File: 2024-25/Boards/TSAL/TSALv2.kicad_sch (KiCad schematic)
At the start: 21 parts, among them J1 043045-0412, Q1 BS250P, Q2 BS170, Q3 UJ3N120035K3S, Q4 BS170, U1 H11L1M

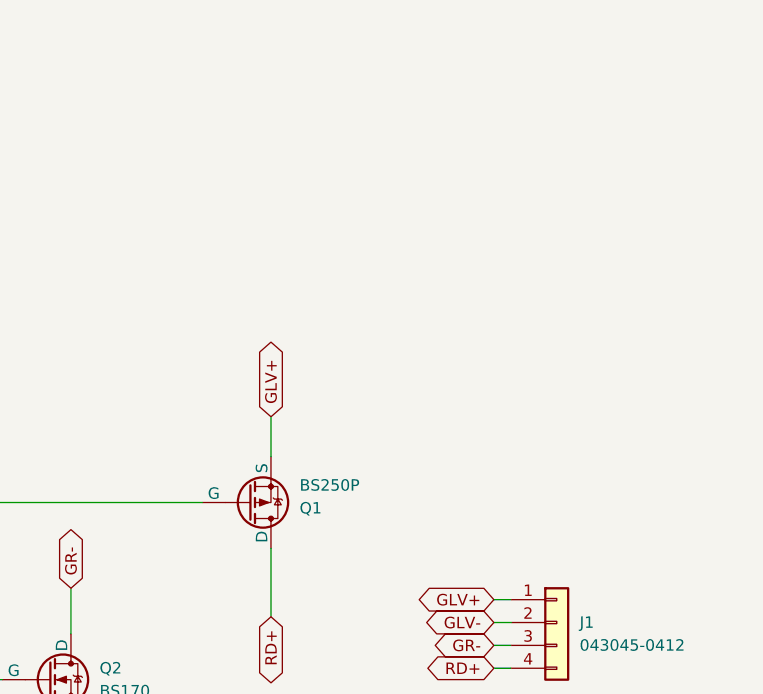
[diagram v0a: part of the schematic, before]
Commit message: added to schematic light flash
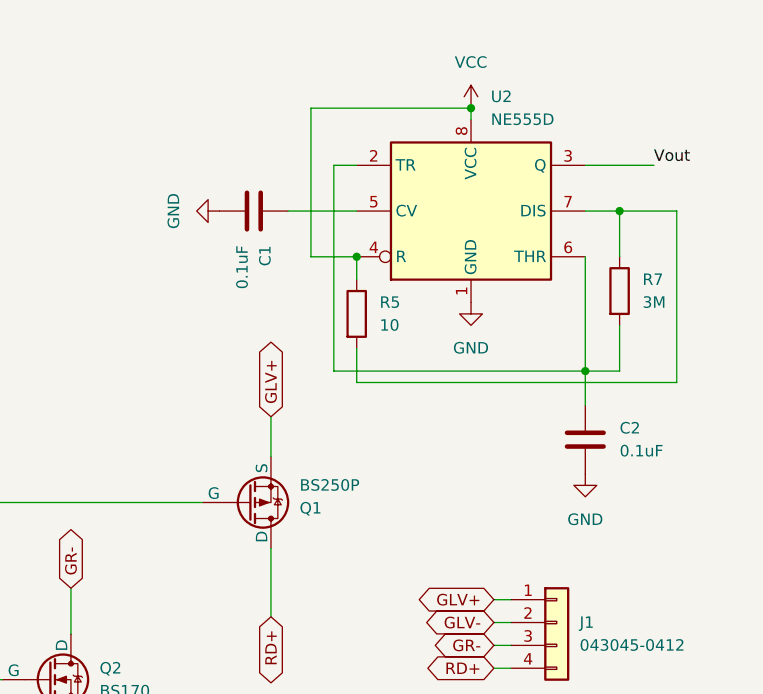
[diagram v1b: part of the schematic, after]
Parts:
- added C1, C2: 0.1uF, symbol Device:C
- added R5: 10, symbol Device:R
- added R7: 3M, symbol Device:R
- added U2: NE555D, Package_SO:SOIC-8_3.9x4.9mm_P1.27mm, symbol Timer:NE555D
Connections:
- new net: C1.2, U2.5 (CV)
- new net: C2.2, R7.2, U2.2 (TR), U2.6 (THR)
- new net: R5.2, R7.1, U2.7 (DIS)
- new net GND: C1.1, C2.1, U2.1 (GND)
- new net VCC: R5.1, U2.4 (R), U2.8 (VCC)
- new net Vout: U2.3 (Q)

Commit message: Board should be ready for pcb
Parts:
- removed Q2: BS170, Package_TO_SOT_THT:TO-92, symbol Simulation_SPICE:NMOS
- added C3: 1uF, Capacitor_SMD:C_0805_2012Metric_Pad1.18x1.45mm_HandSolder, symbol Device:C
- added C4: .1uF, Capacitor_SMD:C_0402_1005Metric_Pad0.74x0.62mm_HandSolder, symbol Device:C
- added R4: 1k, symbol Device:R
- added R8: 10k, symbol Device:R
- C2: value 0.1uF -> 100uF
- R5: value 10 -> 100
- R7: value 3M -> 3k
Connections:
- net VCC is gone; now on net GLV+: R5.1, U2.4 (R), U2.8 (VCC)
- net Vout is gone; now on net Light+: U2.3 (Q)
- net GLV+: now also Q1.1 (D), C3.2, C4.2, R4.1, R8.2
- net GLV-: no longer U1.5
- net GND: now also U1.5, C3.1, C4.1, R8.1
- net GR- renamed Light-
- net RD+ renamed Light+
- net Light+: now also R4.2; no longer Q1.1 (D)
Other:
- note removed: "LED+"
- note removed: "LED-"
- moved on the sheet: C1, C2, D10, D2, D3, D4, D5, D6, D7, D8, D9, J1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

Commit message: Add files via upload
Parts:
- removed C4: .1uF, Capacitor_SMD:C_0402_1005Metric_Pad0.74x0.62mm_HandSolder, symbol Device:C
- removed D10, D2, D3, D4, D5, D6, D7, D8, D9: BZT52-B5V6X, Diode_SMD:D_SOD-123, symbol Device:D_Zener
- removed Q1: BS250P, Package_TO_SOT_THT:TO-92, symbol Simulation_SPICE:PMOS
- removed Q4: BS170, Package_TO_SOT_THT:TO-92, symbol Simulation_SPICE:NMOS
- added D2: BZT52C12, Diode_SMD:D_SOD-123F, symbol Diode:BZT52Bxx
- added Q1: DMP2035U-7, SOT23_DIO, symbol Transistor_FET:DMP2035U-7
- added Q4: DMN2056U, Package_TO_SOT_SMD:SOT-23, symbol Transistor_FET:DMN2056U
- C1, C2: footprint (none) -> Capacitor_SMD:C_0805_2012Metric_Pad1.18x1.45mm_HandSolder
- Q3: value UJ3N120035K3S -> UJ3N065080K3S
- R1, R2, R3, R6: footprint Resistor_THT:R_Axial_DIN0207_L6.3mm_D2.5mm_P7.62mm_Horizontal -> Resistor_SMD:R_0805_2012Metric_Pad1.20x1.40mm_HandSolder
- R4, R5, R7, R8: footprint (none) -> Resistor_SMD:R_0805_2012Metric_Pad1.20x1.40mm_HandSolder
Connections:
- net GLV- is gone; now on net GND: J1.2 (Pin_2)
- net Light- is gone; now on net Light+: J1.3 (Pin_3)
- net GLV+: now also Q1.2 (S); no longer R5.1, R8.2, U2.4 (R)
- net HV+: now also D2.1 (K)
- net HV-: now also Q4.2 (S)
- net Light+: no longer J1.4 (Pin_4)
- net at R2.1: now also D2.2 (A)
- net at D1.1 (K), R2.2, R3.1: now also Q4.1 (G)
- net at U1.2: now also Q4.3 (D)
- net at R1.2, U1.4: now also Q1.1 (G)
- new net: Q1.3 (D), R5.1, R8.2, U2.4 (R)
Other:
- note removed: "Connect negative side of green LED to board and positive side of red LED"
- moved on the sheet: J1, Molex1, R8

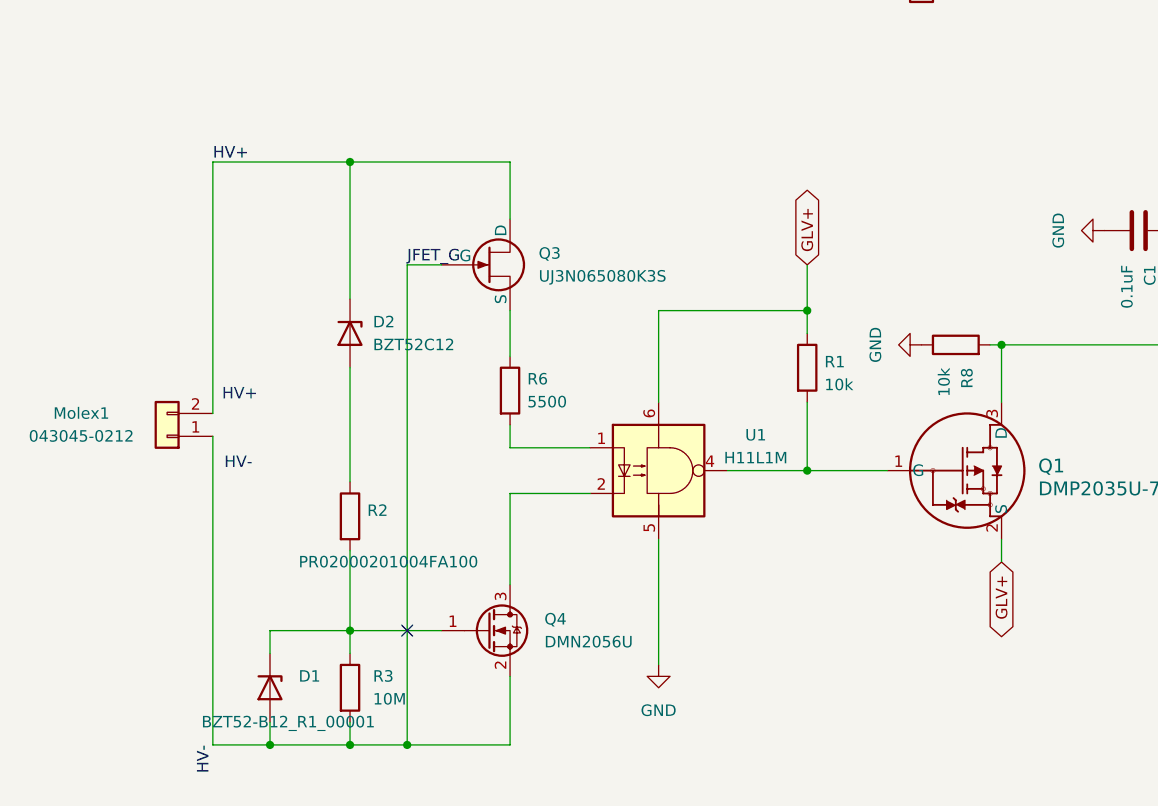
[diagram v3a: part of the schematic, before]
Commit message: split up TSAL resistors for voltage rating
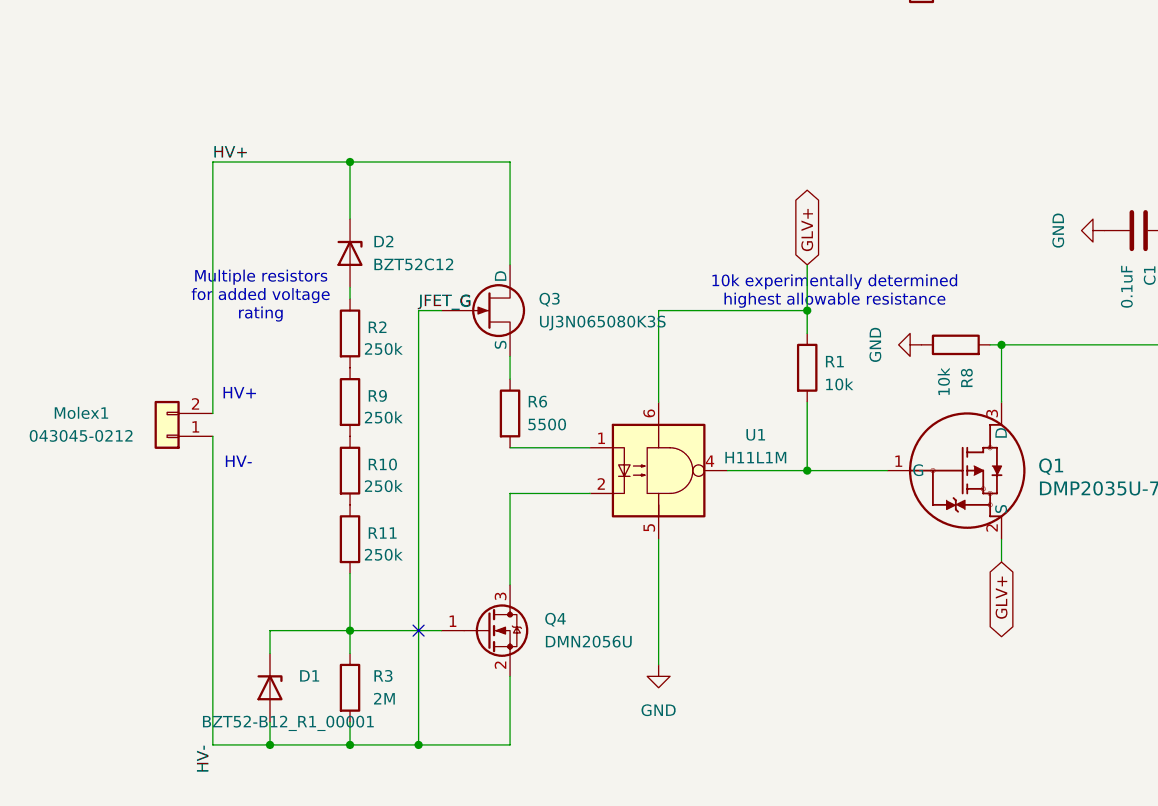
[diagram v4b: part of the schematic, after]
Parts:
- added R10, R11, R9: 250k, Resistor_SMD:R_0805_2012Metric_Pad1.20x1.40mm_HandSolder, symbol Device:R
- R2: value PR02000201004FA100 -> 250k
- R3: value 10M -> 2M
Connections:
- net at D1.1 (K), Q4.1 (G), R3.1: now also R11.2; no longer R2.2
- new net: R2.2, R9.1
- new net: R10.1, R9.2
- new net: R10.2, R11.1
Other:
- note added: "10k experimentally determined highest allowable resistance"
- note added: "Multiple resistors for added voltage rating"
- moved on the sheet: D2, Q3, R2, R6

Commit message: updated documentation
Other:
- note added: "NE555 Timer at ~3.3 Hz"
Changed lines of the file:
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@@
+		)
+	)
+	(text "NE555 Timer at ~3.3 Hz"
+		(exclude_from_sim no)
+		(at 163.576 25.4 0)
+		(effects
+			(font
+				(size 1.27 1.27)
+			)
 		)
 	)

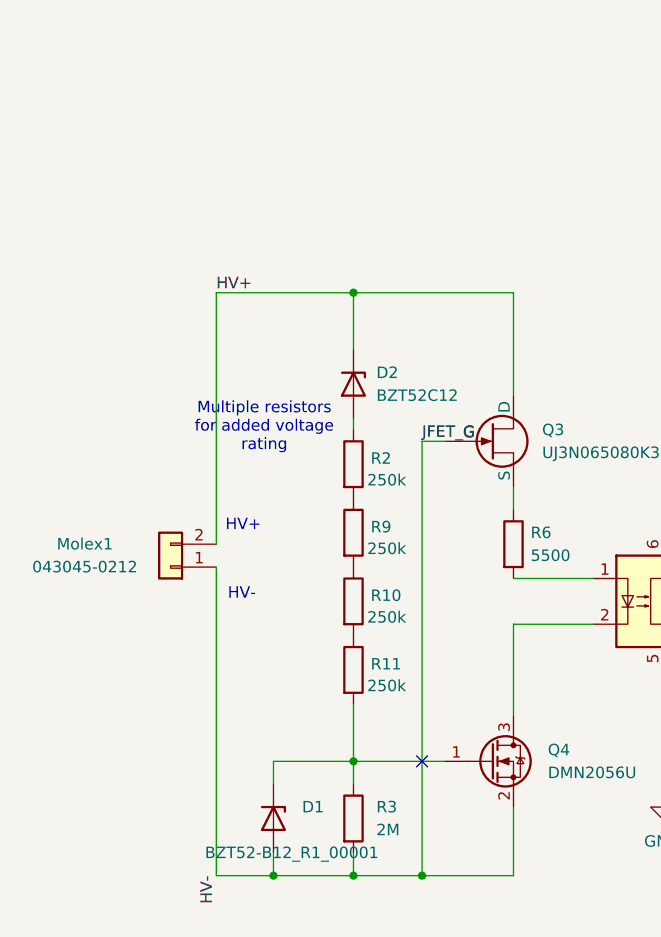
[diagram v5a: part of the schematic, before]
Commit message: updated resistors to be smd on VIL and added fuses and mounting holes to TSAL
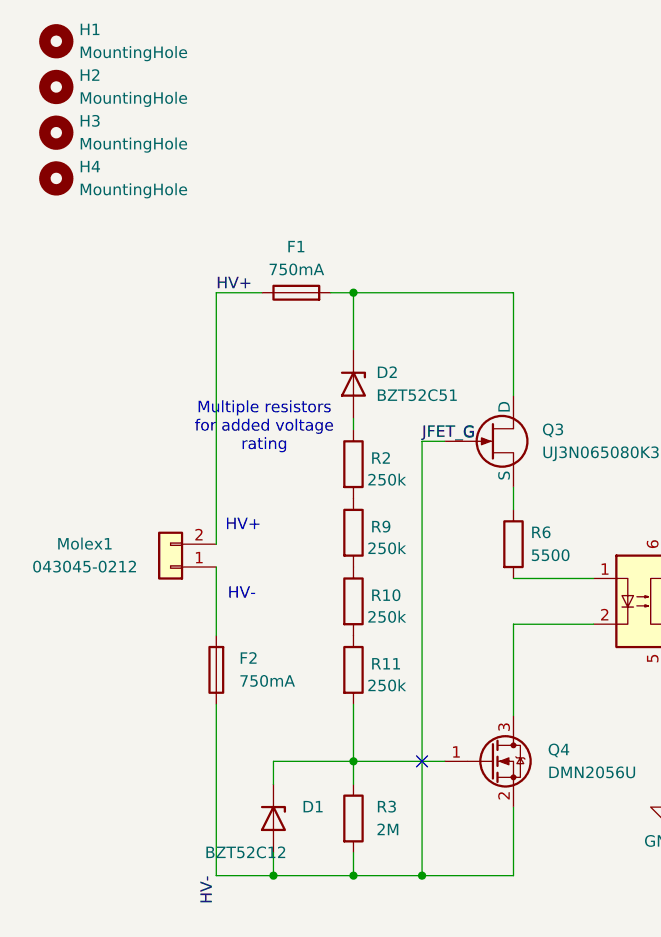
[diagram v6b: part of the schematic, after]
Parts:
- added F1, F2: 750mA, Library:FUSE_BK_PCS, symbol Device:Fuse
- added H1, H2, H3, H4: MountingHole, MountingHole:MountingHole_4.3mm_M4, symbol Mechanical:MountingHole
- D1: value BZT52-B12_R1_00001 -> BZT52C12
- D2: value BZT52C12 -> BZT52C51
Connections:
- net HV+: now also F1.1; no longer D2.1 (K), Q3.2 (D)
- net HV-: now also F2.1; no longer Molex1.1 (Pin_1)
- new net: D2.1 (K), F1.2, Q3.2 (D)
- new net: F2.2, Molex1.1 (Pin_1)

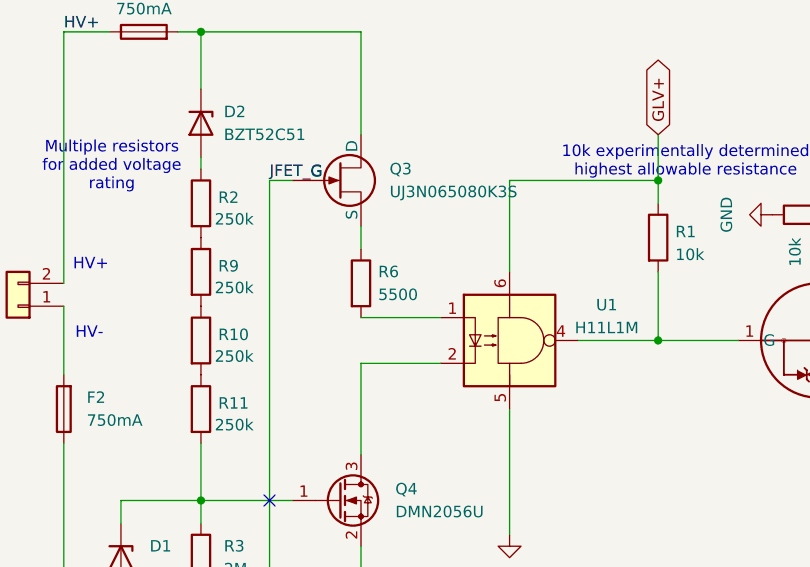
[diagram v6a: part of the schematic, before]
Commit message: updated names of parts
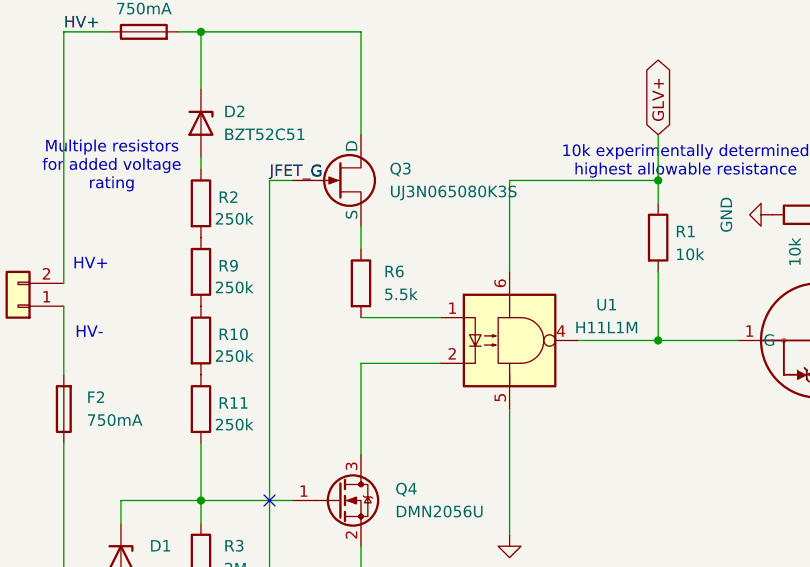
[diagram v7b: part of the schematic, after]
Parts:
- R6: value 5500 -> 5.5k
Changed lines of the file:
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@@
 		(fields_autoplaced yes)
 		(property "Reference" "R6"
-			(at 71.755 78.74 0)
+			(at 72.39 78.7399 0)
 			(effects
 				(font
@@
 			)
 		)
-		(property "Value" "5500"
-			(at 71.755 81.28 0)
+		(property "Value" "5.5k"
+			(at 72.39 81.2799 0)
 			(effects
 				(font
